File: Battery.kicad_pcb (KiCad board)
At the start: 2 copper layers, 85.5 x 25 mm, 47 parts, among them J1 BATTERY, J2 CHG, J3 PWR, J4 3v3, J5 1v8, J6 NTC, Q1 Si9933CDY, U1 BQ29200, U2 LTC4002ES8, U3 MAX604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

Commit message: Redraw board and plot Gerbers
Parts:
- moved TP12 6.26 mm to (241.5, 44.0)
- moved C2 4.00 mm to (194.5, 49.0)
- moved C3 4.00 mm to (192.5, 53.0)
- moved C5 4.00 mm to (198.0, 55.0)
- moved C8 4.00 mm to (201.5, 52.0)
- moved R2 4.00 mm to (191.5, 48.0)
- moved R3 4.00 mm to (191.5, 50.0)
- moved R4 4.00 mm to (194.5, 53.0)
- moved R6 4.00 mm to (202.5, 49.0)
- moved TP1 4.00 mm to (193.0, 44.0)
- moved TP2 4.00 mm to (196.5, 44.0)
- moved TP3 4.00 mm to (201.0, 44.0)
- moved U1 4.00 mm to (198.0, 51.5)
- moved TP13 3.91 mm to (223.5, 60.2)
- moved J1 3.50 mm to (183.5, 55.5)
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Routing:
- net GND: track 125.5 -> 118.8 mm, vias 39 -> 40
- net Net-(J2-Pad1): track 47.6 -> 52.3 mm
- net /BATT_MON: track 24.1 -> 25.3 mm
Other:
- board size 85.5 x 25 mm -> 90 x 25 mm
- board text added: "NTC"
- board text added: "VBATT"

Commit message: Add back silkscreen text
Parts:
- added G***: LOGO, Battery:cusf_logo_full, B.Cu at (224.0, 53.0)
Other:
- board text added: "2S Li-Ion Battery Charger H. Franks"

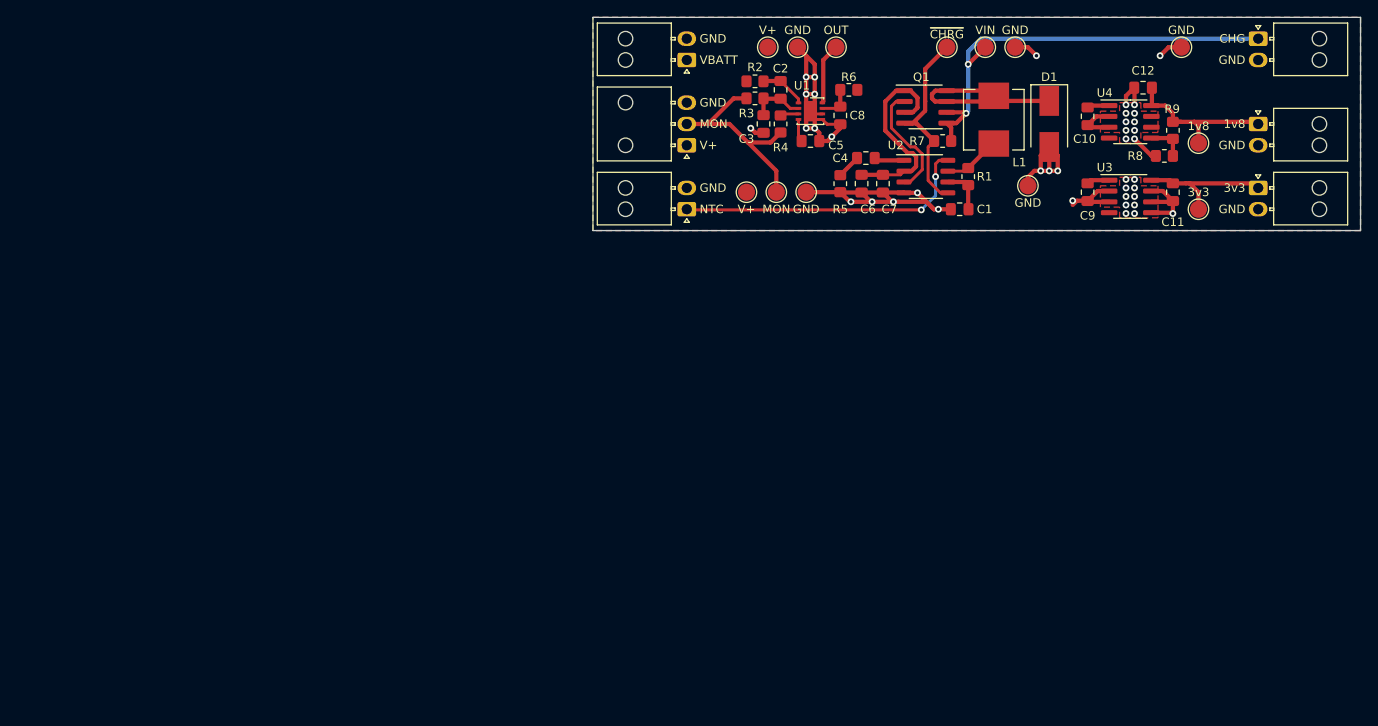
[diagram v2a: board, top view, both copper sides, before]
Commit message: Fix sense resistor and resize board
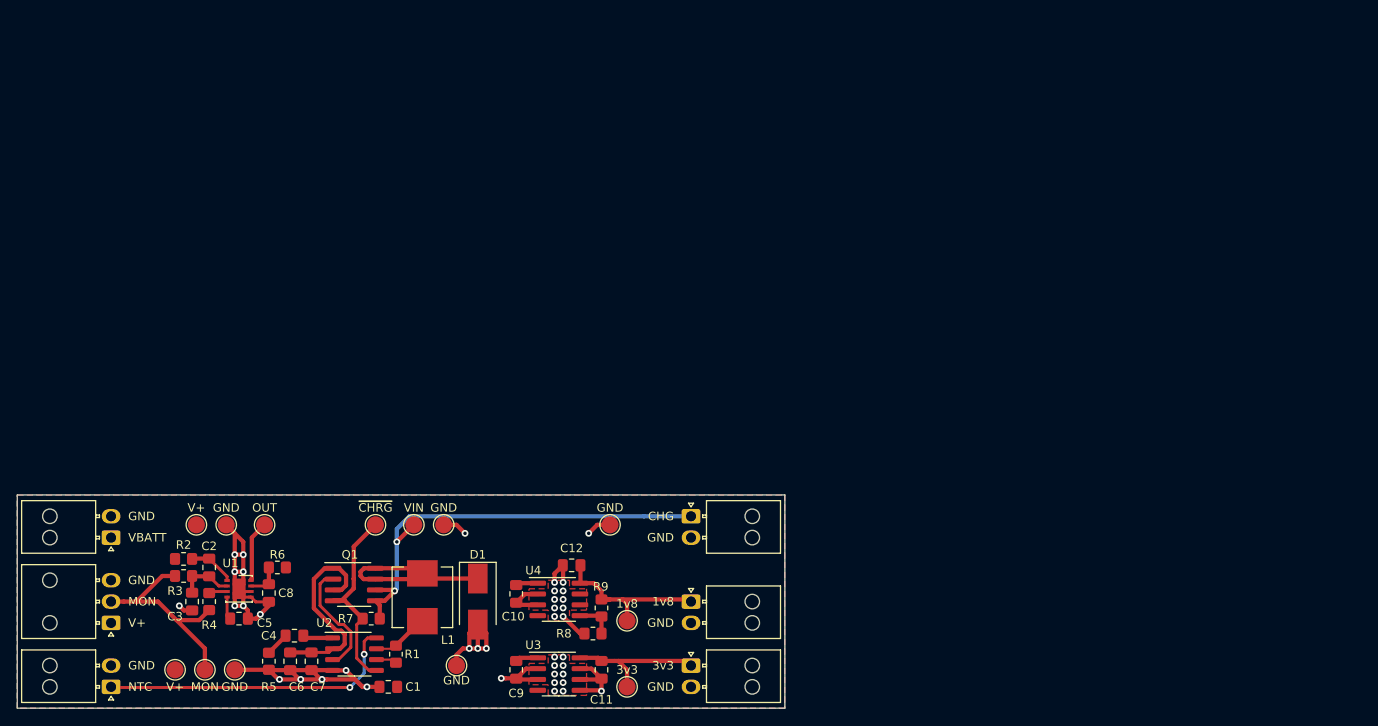
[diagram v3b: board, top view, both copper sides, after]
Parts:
- moved G*** 88.0 mm to (156.5, 109.5)
- moved J1 87.7 mm to (116.0, 111.5)
- moved J3 87.7 mm to (116.0, 101.5)
- moved J6 87.7 mm to (116.0, 119.0)
- moved TP13 87.5 mm to (156.5, 116.5)
- moved R1 87.4 mm to (149.4, 115.2)
- moved C1 87.3 mm to (148.5, 119.0)
- moved C11 87.3 mm to (173.5, 117.0)
- moved C12 87.3 mm to (170.0, 104.8)
- moved C2 87.3 mm to (127.5, 105.0)
- moved C3 87.3 mm to (125.5, 109.0)
- moved C4 87.3 mm to (137.5, 113.0)
- moved C5 87.3 mm to (131.0, 111.0)
- moved C6 87.3 mm to (137.0, 116.0)
- moved C7 87.3 mm to (139.5, 116.0)
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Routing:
- net VBATT: track 10.7 -> 7.78 mm
- net Net-(J6-Pad1): track 35.2 -> 35.7 mm
- net 1v8: track 19.8 -> 20.3 mm
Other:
- rule trace_min: 0.3 -> 0.25
- board text added: "2S Li-Ion Battery Charger H. E. Franks"
- board text removed: "2S Li-Ion Battery Charger H. Franks"
